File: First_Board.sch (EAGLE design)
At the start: 45 parts, among them U0 F22X4---DA38, U1 TLC59108PW, U3 A1101, U4 TPS62111RSA

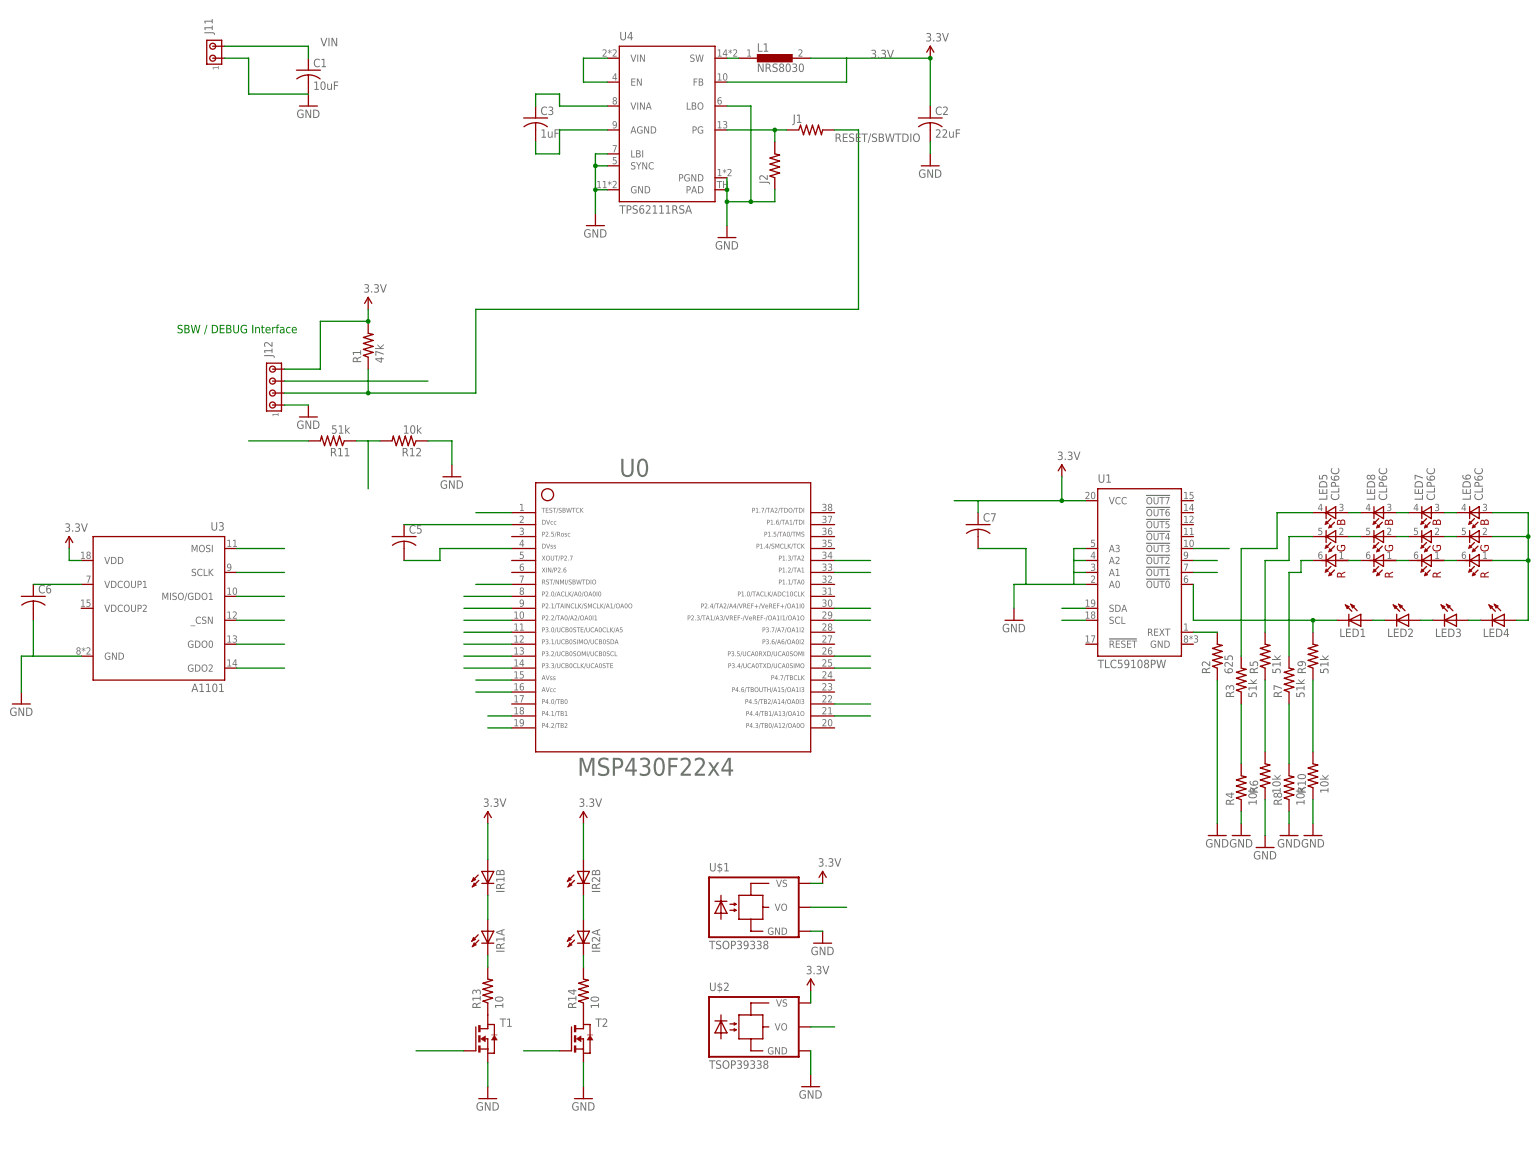
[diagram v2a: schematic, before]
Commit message: Adding IR LED/Detector (and maybe the bottom RGB leds if not already committed
git-svn-id: file:///p/svn/Projects/Boards/Driveway_Lights@60 1e7840b9-f7c2-db11-b69c-00d0b71b9132
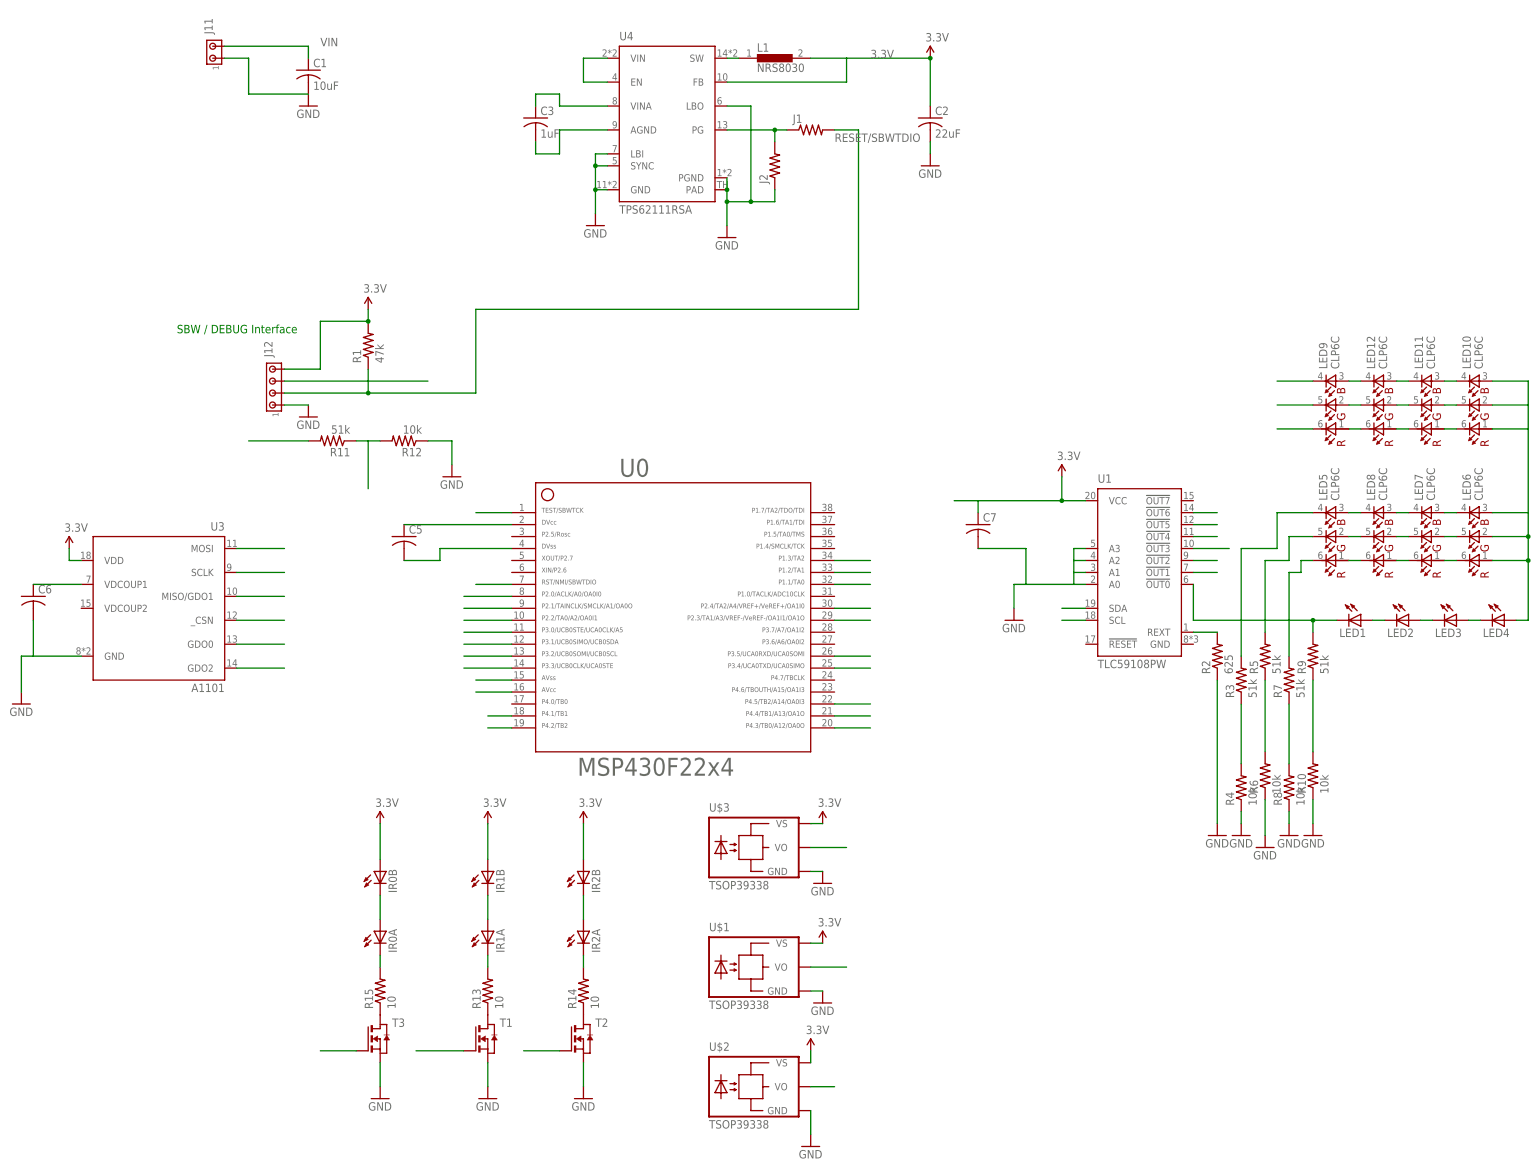
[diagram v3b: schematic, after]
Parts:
- added IR0A, IR0B: (no value), led:LED5MM
- added LED10, LED11, LED12, LED9: CLP6C, led:CLP6C
- added R15: 10, rcl:R-US_R0603
- added T3: (no value), zetex:NMOSSOT23
- added U$3: TSOP39338, opto-vishay:TSOP39338
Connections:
- new net BLUE2: LED9.BC, U1.!OUT6
- new net GREEN2: LED9.GC, U1.!OUT5
- new net IRLED0: T3.G, U0.20
- new net IR_IN0: U$3.VO, U0.32
- new net N$12: LED12.BC, LED9.BA
- new net N$13: LED11.BC, LED12.BA
- new net N$14: LED10.BC, LED11.BA
- new net N$15: LED10.GC, LED11.GA
- new net N$16: LED11.GC, LED12.GA
- new net N$17: LED12.GC, LED9.GA
- new net N$18: LED12.RC, LED9.RA
- new net N$20: LED11.RC, LED12.RA
- new net N$21: LED10.RC, LED11.RA
- new net N$22: IR0A.C, R15.2
- new net N$23: IR0A.A, IR0B.C
- new net N$24: R15.1, T3.D
- new net RED2: LED9.RC, U1.!OUT4
- net 3.3V: now also IR0B.A, U$3.VS
- net GND: now also T3.S, U$3.GND
- net VIN: now also LED10.BA, LED10.GA, LED10.RA
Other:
- moved on the sheet: U$1, U$2
